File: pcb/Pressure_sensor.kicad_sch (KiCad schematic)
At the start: 6 parts, among them J18 Conn_03x01, U8 DPS310XTSA1

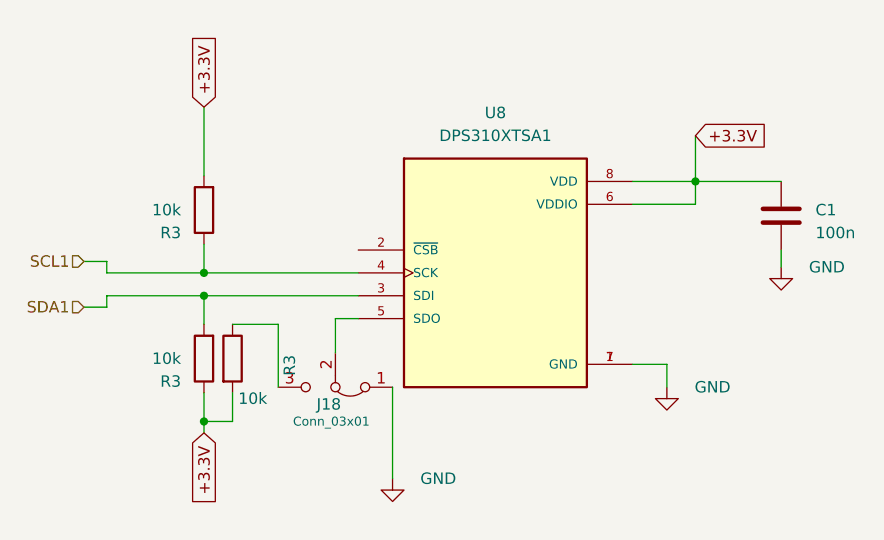
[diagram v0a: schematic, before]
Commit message: feat: Reorganize PCB project
Include all 3D step files
Refactor all folders for symbolds and footprints
Add missing datasheets
Link all symbols in KiCad projects
Rename the project to SensEdu
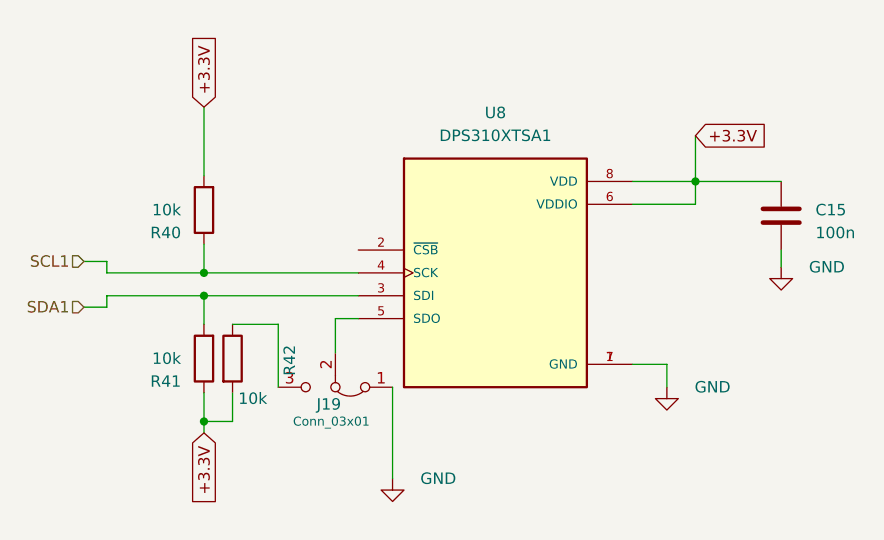
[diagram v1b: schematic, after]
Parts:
- renumbered C1 to C15, J18 to J19, R3 to R40, R3 to R41, R3 to R42
